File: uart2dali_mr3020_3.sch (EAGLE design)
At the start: 81 parts, among them IC2 LM393D, IC3 SFH6156, IC4 SFH6156, J1 AVR_SPI_PRG_6NS, Q1 SST201, Q2 BSP170P, Q3 BC817-25SMD, X2 22-23-2021

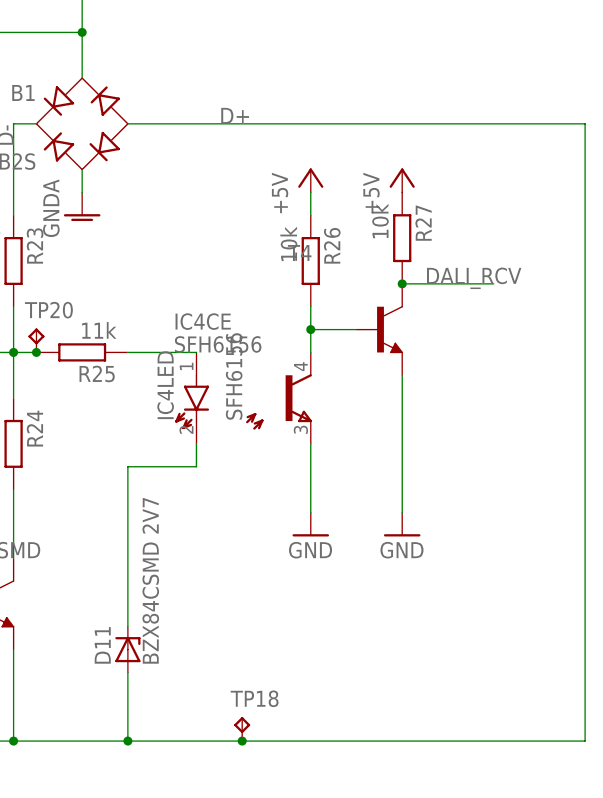
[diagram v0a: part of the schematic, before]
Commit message: - added some comments - fixes on layout
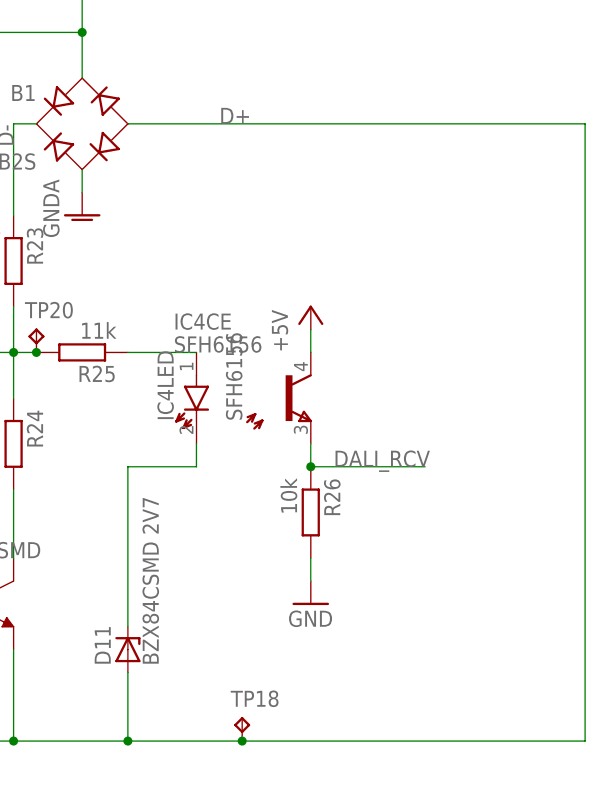
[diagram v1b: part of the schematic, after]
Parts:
- removed R27: 10k, resistor:R-EU_R0603
- removed T4: (no value), transistor:MMBT3904LT1-NPN-SOT23-BEC
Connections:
- new net N$7: IC4CE.E, R26.1
- net +5V: now also IC4CE.C; no longer R26.1, R27.1
- net DALI_RCV: no longer IC4CE.C, R26.2, R27.2, T4.B, T4.C
- net GND: now also R26.2; no longer IC4CE.E, T4.E
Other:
- moved on the sheet: R26
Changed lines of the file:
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@@
 <part name="VDD5" library="supply1" deviceset="VDD" device=""/>
 <part name="VDD6" library="supply1" deviceset="VDD" device=""/>
-<part name="T4" library="transistor" deviceset="*-NPN-" device="SOT23-BEC" technology="MMBT3904LT1"/>
-<part name="R27" library="resistor" deviceset="R-EU_" device="R0603" value="10k"/>
-<part name="P+3" library="supply1" deviceset="+5V" device=""/>
-<part name="GND33" library="supply1" deviceset="GND" device=""/>
 <part name="X2" library="con-molex" deviceset="22-23-2021" device=""/>
 <part name="J2" library="con-jack" deviceset="JACK-PLUG" device="1"/>
@@
 <instance part="C12" gate="G$1" x="518.16" y="43.18"/>
 <instance part="R20" gate="G$1" x="485.14" y="68.58" rot="R270"/>
-<instance part="GND2" gate="1" x="566.42" y="50.8"/>
-<instance part="R26" gate="G$1" x="566.42" y="81.28" rot="R270"/>
-<instance part="P+1" gate="1" x="566.42" y="91.44"/>
+<instance part="GND2" gate="1" x="566.42" y="43.18"/>
+<instance part="R26" gate="G$1" x="566.42" y="53.34" rot="R270"/>
+<instance part="P+1" gate="1" x="566.42" y="76.2"/>
 <instance part="P+2" gate="1" x="492.76" y="81.28"/>
 <instance part="C7" gate="G$1" x="215.9" y="27.94" rot="R180"/>
@@
 <instance part="VDD5" gate="G$1" x="17.78" y="116.84"/>
 <instance part="VDD6" gate="G$1" x="25.4" y="116.84"/>
-<instance part="T4" gate="G$1" x="574.04" y="73.66"/>
-<instance part="R27" gate="G$1" x="576.58" y="83.82" rot="R270"/>
-<instance part="P+3" gate="1" x="576.58" y="91.44"/>
-<instance part="GND33" gate="1" x="576.58" y="50.8"/>
 <instance part="X2" gate="-1" x="487.68" y="114.3" rot="R180"/>
 <instance part="X2" gate="-2" x="487.68" y="109.22" rot="R180"/>
@@
 <net name="GND" class="0">
 <segment>
-<pinref part="IC4" gate="CE" pin="E"/>
-<pinref part="GND2" gate="1" pin="GND"/>
-<wire x1="566.42" y1="60.96" x2="566.42" y2="53.34" width="0.1524" layer="91"/>
-</segment>
-<segment>
 <pinref part="C7" gate="G$1" pin="1"/>
 <pinref part="GND9" gate="1" pin="GND"/>
@@
 </segment>
 <segment>
-<pinref part="T4" gate="G$1" pin="E"/>
-<pinref part="GND33" gate="1" pin="GND"/>
-<wire x1="576.58" y1="53.34" x2="576.58" y2="68.58" width="0.1524" layer="91"/>
-</segment>
-<segment>
 <pinref part="R29" gate="G$1" pin="1"/>
 <pinref part="GND3" gate="1" pin="GND"/>
 </segment>
+<segment>
+<pinref part="R26" gate="G$1" pin="2"/>
+<pinref part="GND2" gate="1" pin="GND"/>
+<wire x1="566.42" y1="48.26" x2="566.42" y2="45.72" width="0.1524" layer="91"/>
+</segment>
 </net>
 <net name="+5V" class="0">
-<segment>
-<pinref part="P+1" gate="1" pin="+5V"/>
-<pinref part="R26" gate="G$1" pin="1"/>
-<wire x1="566.42" y1="88.9" x2="566.42" y2="86.36" width="0.1524" layer="91"/>
-</segment>
 <segment>
 <pinref part="IC3" gate="LED" pin="A"/>
@@
 </segment>
 <segment>
-<pinref part="R27" gate="G$1" pin="1"/>
-<pinref part="P+3" gate="1" pin="+5V"/>
-</segment>
-<segment>
 <pinref part="R28" gate="G$1" pin="2"/>
 <pinref part="P+4" gate="1" pin="+5V"/>
 </segment>
+<segment>
+<pinref part="P+1" gate="1" pin="+5V"/>
+<pinref part="IC4" gate="CE" pin="C"/>
+<wire x1="566.42" y1="73.66" x2="566.42" y2="71.12" width="0.1524" layer="91"/>
+</segment>
 </net>
 <net name="DALI_RCV" class="0">
-<segment>
-<pinref part="R26" gate="G$1" pin="2"/>
-<pinref part="IC4" gate="CE" pin="C"/>
-<wire x1="566.42" y1="76.2" x2="566.42" y2="73.66" width="0.1524" layer="91"/>
-<pinref part="T4" gate="G$1" pin="B"/>
-<wire x1="566.42" y1="73.66" x2="566.42" y2="71.12" width="0.1524" layer="91"/>
-<wire x1="571.5" y1="73.66" x2="566.42" y2="73.66" width="0.1524" layer="91"/>
-<junction x="566.42" y="73.66"/>
-</segment>
 <segment>
 <pinref part="TP9" gate="G$1" pin="TP"/>
@@
 </segment>
 <segment>
-<pinref part="T4" gate="G$1" pin="C"/>
-<pinref part="R27" gate="G$1" pin="2"/>
-<wire x1="576.58" y1="78.74" x2="586.74" y2="78.74" width="0.1524" layer="91"/>
-<junction x="576.58" y="78.74"/>
-<label x="579.12" y="78.74" size="1.778" layer="95"/>
+<wire x1="566.42" y1="58.42" x2="579.12" y2="58.42" width="0.1524" layer="91"/>
+<label x="568.96" y="58.42" size="1.778" layer="95"/>
 </segment>
 </net>
@@
 </segment>
 </net>
+<net name="N$7" class="0">
+<segment>
+<pinref part="IC4" gate="CE" pin="E"/>
+<pinref part="R26" gate="G$1" pin="1"/>
+<wire x1="566.42" y1="60.96" x2="566.42" y2="58.42" width="0.1524" layer="91"/>
+<junction x="566.42" y="58.42"/>
+</segment>
+</net>

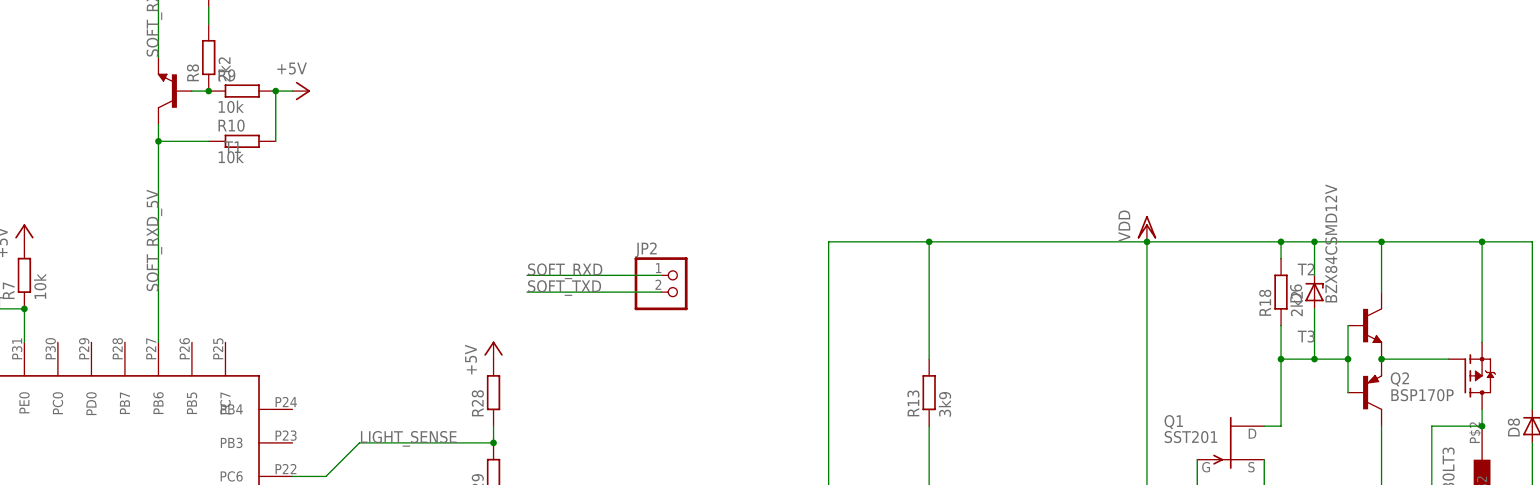
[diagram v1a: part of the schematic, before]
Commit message: - updated schematics and layout - some bugfixes in firmware
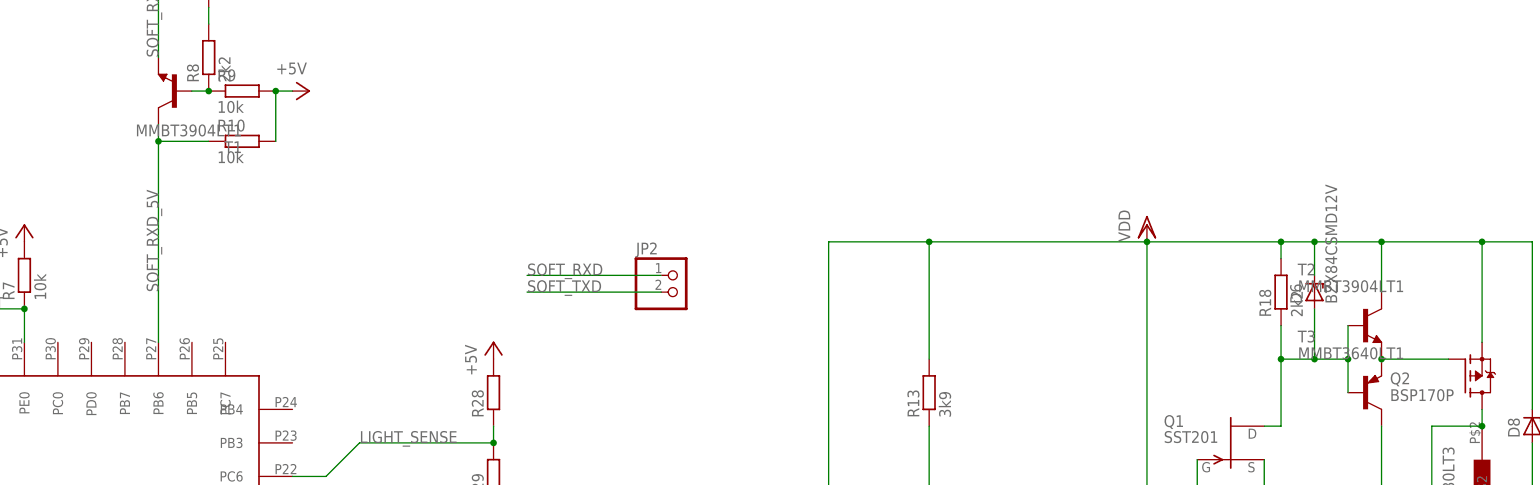
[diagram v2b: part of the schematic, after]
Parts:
- T1, T2: value (none) -> MMBT3904LT1
- T3: value (none) -> MMBT3640LT1
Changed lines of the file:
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@@
 <?xml version="1.0" encoding="utf-8"?>
 <!DOCTYPE eagle SYSTEM "eagle.dtd">
-<eagle version="6.3">
+<eagle version="6.4">
 <drawing>
 <settings>
@@
 <part name="R10" library="resistor" deviceset="R-EU_" device="R0603" value="10k"/>
 <part name="R8" library="resistor" deviceset="R-EU_" device="R0603" value="2k2"/>
-<part name="T1" library="transistor" deviceset="*-NPN-" device="SOT23-BEC" technology="MMBT3904LT1"/>
+<part name="T1" library="transistor" deviceset="*-NPN-" device="SOT23-BEC" technology="MMBT3904LT1" value="MMBT3904LT1"/>
 <part name="GND20" library="supply1" deviceset="GND" device=""/>
 <part name="P+11" library="supply1" deviceset="+5V" device=""/>
 <part name="IC2" library="linear" deviceset="LM393" device="D"/>
-<part name="T3" library="transistor" deviceset="*-PNP-" device="SOT23-BEC" technology="MMBT3640LT1"/>
-<part name="T2" library="transistor" deviceset="*-NPN-" device="SOT23-BEC" technology="MMBT3904LT1"/>
+<part name="T3" library="transistor" deviceset="*-PNP-" device="SOT23-BEC" technology="MMBT3640LT1" value="MMBT3640LT1"/>
+<part name="T2" library="transistor" deviceset="*-NPN-" device="SOT23-BEC" technology="MMBT3904LT1" value="MMBT3904LT1"/>
 <part name="Q2" library="transistor-fet" deviceset="BSP170P" device=""/>
 <part name="Q1" library="transistor-fet" deviceset="?20*" device="SST" technology="1"/>
